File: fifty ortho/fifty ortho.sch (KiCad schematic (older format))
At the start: 115 parts, among them J1 Conn_01x01, J2 Conn_01x01, J3 Conn_01x01, SW1 SW_PUSH, U1 ProMicro

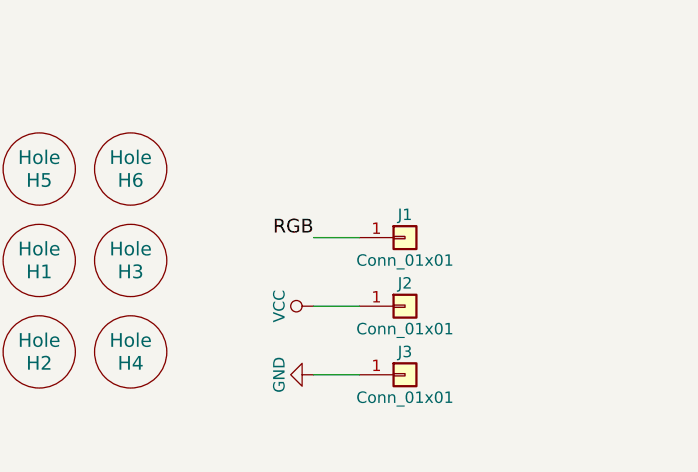
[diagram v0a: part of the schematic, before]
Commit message: push pcb with updated correct footprint
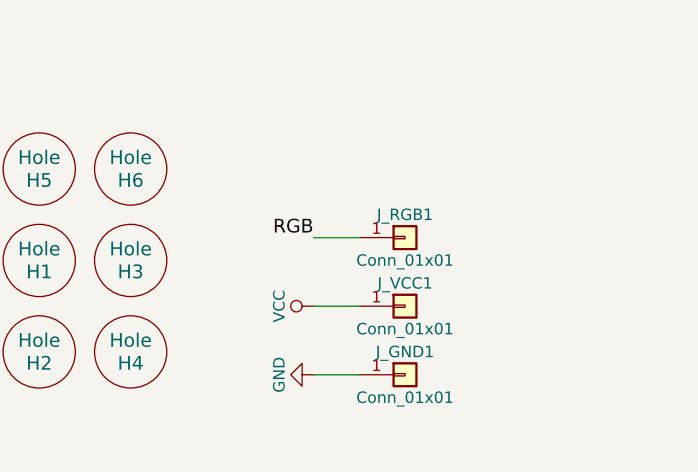
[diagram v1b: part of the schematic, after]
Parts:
- U1: footprint keebs:Pro_Micro -> keebs:Pro_Micro Correct PinOut
- renumbered J3 to J_GND1, J1 to J_RGB1, J2 to J_VCC1
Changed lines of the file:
@@
 F 0 "U1" H 2100 6500 60  0000 C CNN
 F 1 "ProMicro" H 2100 5750 60  0000 C CNN
-F 2 "keebs:Pro_Micro" V 3150 4000 60  0001 C CNN
+F 2 "keebs:Pro_Micro Correct PinOut" V 3150 4000 60  0001 C CNN
 F 3 "" V 3150 4000 60  0001 C CNN
 	1    2100 6500
@@
 $EndComp
 $Comp
-L Conn_01x01 J1
+L Conn_01x01 J_RGB1
 U 1 1 5B4CBC51
 P 5800 6750
-F 0 "J1" H 5800 6850 50  0000 C CNN
+F 0 "J_RGB1" H 5800 6850 50  0000 C CNN
 F 1 "Conn_01x01" H 5800 6650 50  0000 C CNN
 F 2 "Connectors:Pin_d0.9mm_L10.0mm_W2.4mm_FlatFork" H 5800 6750 50  0001 C CNN
@@
 $EndComp
 $Comp
-L Conn_01x01 J3
+L Conn_01x01 J_GND1
 U 1 1 5B4CBFC1
 P 5800 7350
-F 0 "J3" H 5800 7450 50  0000 C CNN
+F 0 "J_GND1" H 5800 7450 50  0000 C CNN
 F 1 "Conn_01x01" H 5800 7250 50  0000 C CNN
 F 2 "Connectors:Pin_d0.9mm_L10.0mm_W2.4mm_FlatFork" H 5800 7350 50  0001 C CNN
@@
 $EndComp
 $Comp
-L Conn_01x01 J2
+L Conn_01x01 J_VCC1
 U 1 1 5B4CC12F
 P 5800 7050
-F 0 "J2" H 5800 7150 50  0000 C CNN
+F 0 "J_VCC1" H 5800 7150 50  0000 C CNN
 F 1 "Conn_01x01" H 5800 6950 50  0000 C CNN
 F 2 "Connectors:Pin_d0.9mm_L10.0mm_W2.4mm_FlatFork" H 5800 7050 50  0001 C CNN

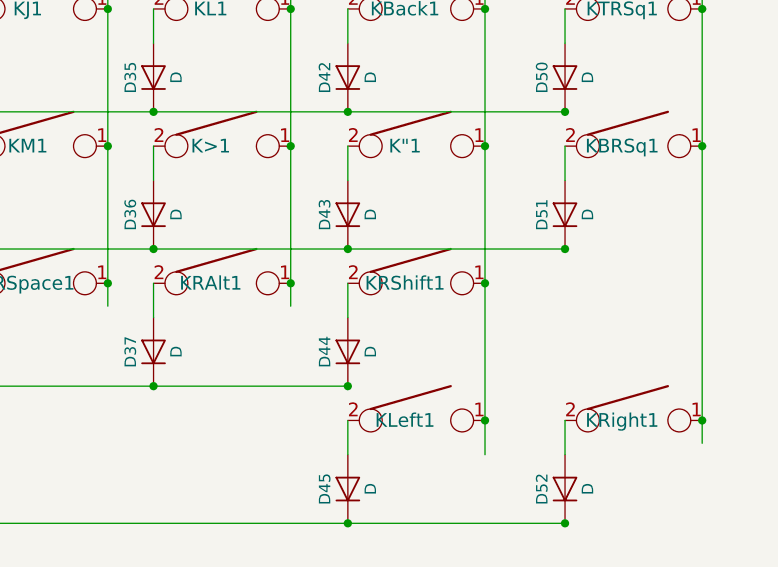
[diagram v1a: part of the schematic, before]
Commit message: changed right shift to enter for default
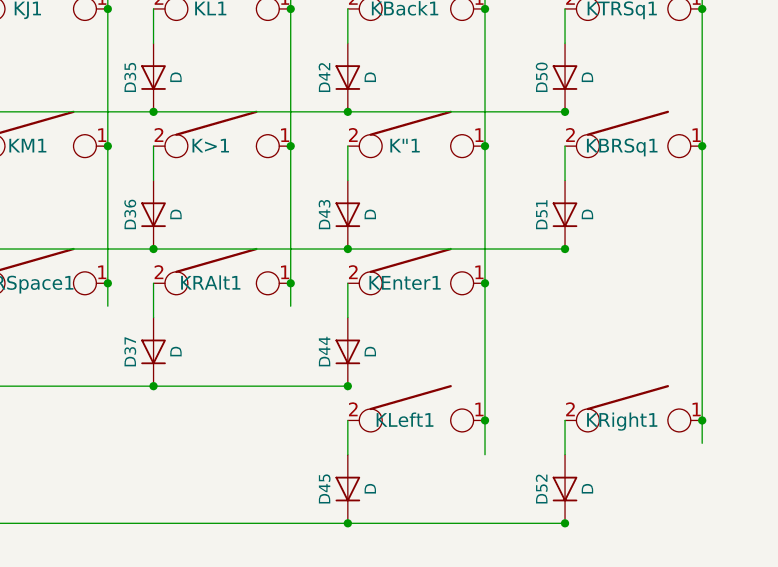
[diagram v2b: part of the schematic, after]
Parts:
- renumbered KRShift1 to KEnter1
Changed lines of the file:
@@
 $EndComp
 $Comp
-L KEYSW KRShift1
+L KEYSW KEnter1
 U 1 1 5B461E8B
 P 5500 4400
-F 0 "KRShift1" H 5450 4400 60  0000 C CNN
+F 0 "KEnter1" H 5450 4400 60  0000 C CNN
 F 1 "KEYSW" H 5500 4300 60  0001 C CNN
 F 2 "keebs:Mx_Alps_100" H 5500 4400 60  0001 C CNN
